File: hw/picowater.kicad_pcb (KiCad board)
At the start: 2 copper layers, 74.3 x 55.5 mm, 19 parts, among them J1 GPIO Pins, J2 Power In, J3 +5V Pins, J4 UART, J5 Power Out, J6 RTC, J7 GPIO2, U1 Pico

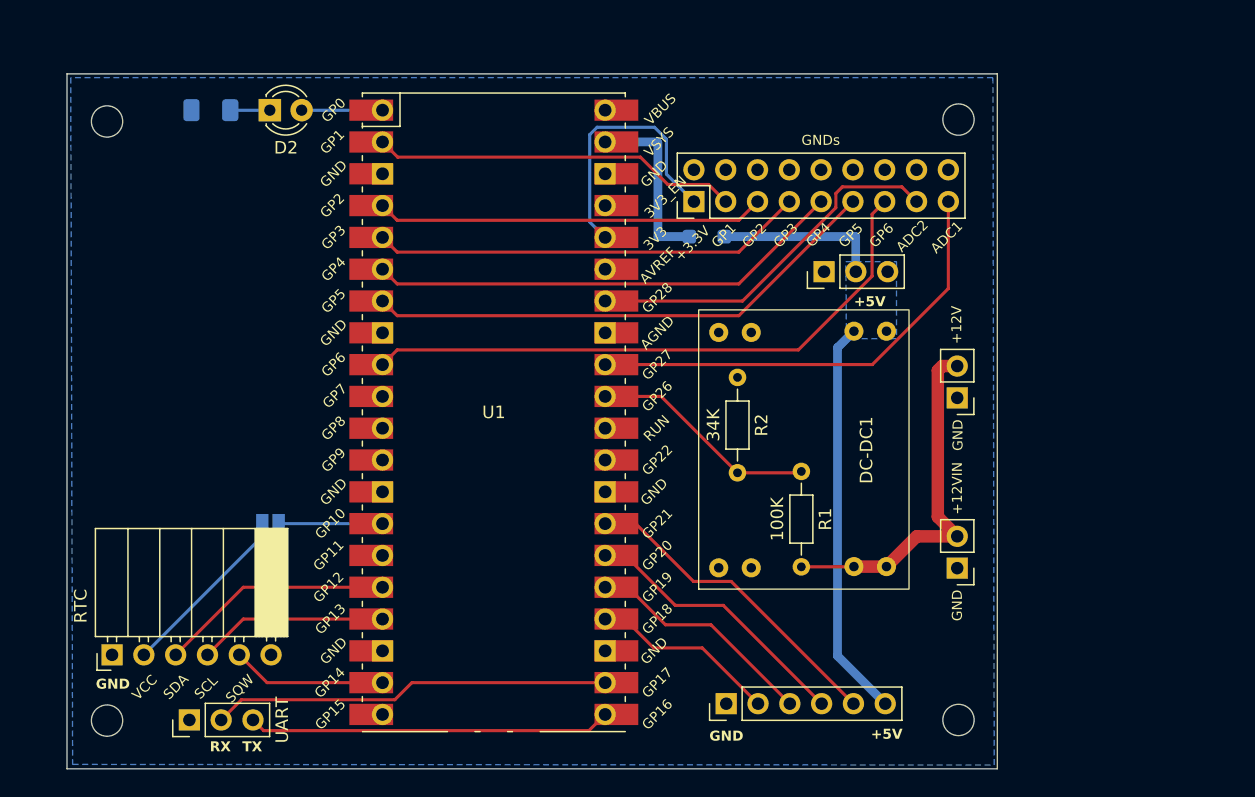
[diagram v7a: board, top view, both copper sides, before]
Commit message: [pcb] new 0.9 release with many changes
- onboard DC-DC converter
- onboard RTC
- onboard Relay circuit
- new connectors
- others
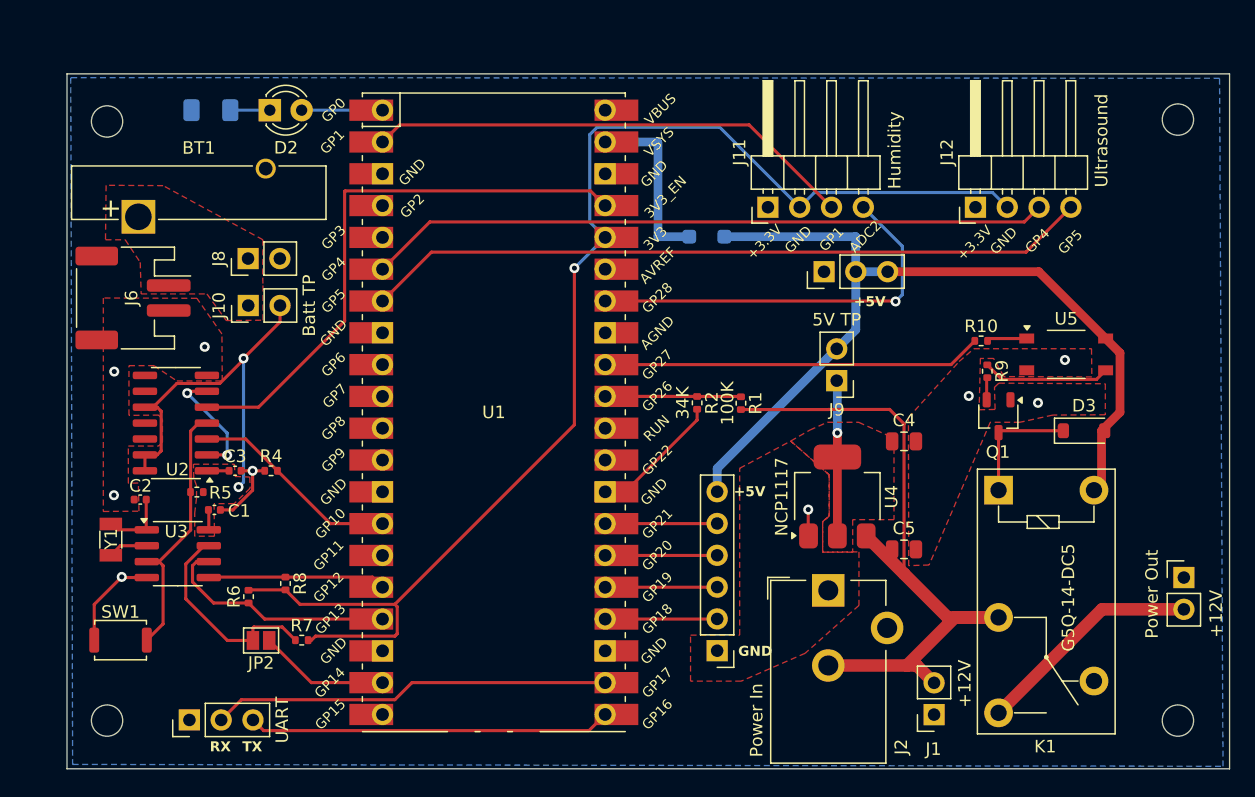
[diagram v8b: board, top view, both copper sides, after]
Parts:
- removed DC-DC1: ~, Lunasys_Library:MP1584EN DC-DC 3A Step-Down
- removed JP1: VCC solder jump, Jumper:SolderJumper-2_P1.3mm_Open_Pad1.0x1.5mm
- added BT1: Battery_Cell, Battery:Battery_Panasonic_CR2032-VS1N_Vertical_CircularHoles, F.Cu at (60.5, 79.5)
- added C1: 100nF, Capacitor_SMD:C_0402_1005Metric, F.Cu at (66.6, 102.9)
- added C2: 22pF, Capacitor_SMD:C_0402_1005Metric, F.Cu at (60.6, 102.1)
- added C3: 100nF, Capacitor_SMD:C_0402_1005Metric, F.Cu at (68.2, 99.8)
- added C4: 10u, Capacitor_SMD:C_0805_2012Metric, F.Cu at (121.7, 97.5)
- added C5: 10u, Capacitor_SMD:C_0805_2012Metric, F.Cu at (121.7, 106.1)
- added D3: 1N4007, Diode_SMD:D_SOD-123, F.Cu at (136.0, 96.6)
- added J10: Batt TP, Connector_PinHeader_2.54mm:PinHeader_1x02_P2.54mm_Vertical, F.Cu at (69.3, 86.6)
- added J11: Humidity, Connector_PinHeader_2.54mm:PinHeader_1x04_P2.54mm_Horizontal, F.Cu at (110.8, 78.8)
- added J12: Ultrasound, Connector_PinHeader_2.54mm:PinHeader_1x04_P2.54mm_Horizontal, F.Cu at (127.4, 78.8)
- added J8: Alt-Bat, Connector_PinHeader_2.54mm:PinHeader_1x02_P2.54mm_Vertical, F.Cu at (69.3, 82.8)
- added J9: 5V TP, Connector_PinHeader_2.54mm:PinHeader_1x02_P2.54mm_Vertical, F.Cu at (116.3, 92.6)
- added JP2: Jmp_CLKOUT, Jumper:SolderJumper-2_P1.3mm_Open_Pad1.0x1.5mm, F.Cu at (70.3, 113.3)
- added K1: G5Q-14-DC5, Relay_THT:Relay_SPDT_Omron-G5Q-1, F.Cu at (129.2, 101.3)
- added Q1: S8050, Package_TO_SOT_SMD:TSOT-23, F.Cu at (129.2, 95.4)
- added R10: 100, Resistor_SMD:R_0402_1005Metric, F.Cu at (127.8, 89.4)
- added R4: 100K, Resistor_SMD:R_0402_1005Metric, F.Cu at (71.1, 99.8)
- added R5: 10K, Resistor_SMD:R_0402_1005Metric, F.Cu at (65.2, 101.5)
- added R6: 10K, Resistor_SMD:R_0402_1005Metric, F.Cu at (69.3, 109.8)
- added R7: 10K, Resistor_SMD:R_0402_1005Metric, F.Cu at (73.5, 113.3)
- added R8: 10K, Resistor_SMD:R_0402_1005Metric, F.Cu at (72.2, 108.8)
- added R9: 220, Resistor_SMD:R_0402_1005Metric, F.Cu at (128.3, 91.8)
- added SW1: SW_Push_SLIM, Button_Switch_SMD:SW_Push_SPST_NO_Alps_SKRK, F.Cu at (59.1, 113.3)
- added U2: SN74HC74N, Package_SO:SOIC-14_3.9x8.7mm_P1.27mm, F.Cu at (63.5, 96.0)
- added U3: PCF8563T, Package_SO:SOIC-8_3.9x4.9mm_P1.27mm, F.Cu at (63.6, 106.4)
- added U4: NCP1117, Package_TO_SOT_SMD:SOT-223-3_TabPin2, F.Cu at (116.3, 101.8)
- added U5: TLP160G, Package_SO:MFSOP6-4_4.4x3.6mm_P1.27mm, F.Cu at (134.6, 90.5)
- added Y1: Crystal, Crystal:Crystal_SMD_3215-2Pin_3.2x1.5mm, F.Cu at (58.3, 105.3)
- J1: value GPIO Pins -> +12V; footprint Connector_PinHeader_2.54mm:PinHeader_2x09_P2.54mm_Vertical -> Connector_PinSocket_2.54mm:PinSocket_1x02_P2.54mm_Vertical
- J2: footprint Connector_PinHeader_2.54mm:PinHeader_1x02_P2.54mm_Vertical -> Connector_BarrelJack:BarrelJack_CUI_PJ-102AH_Horizontal
- J6: value RTC -> JST-PH2 Bat; footprint Connector_PinSocket_2.54mm:PinSocket_1x06_P2.54mm_Horizontal -> Connector_JST:JST_PH_S2B-PH-SM4-TB_1x02-1MP_P2.00mm_Horizontal
- R1, R2: footprint Resistor_THT:R_Axial_DIN0204_L3.6mm_D1.6mm_P7.62mm_Horizontal -> Resistor_SMD:R_0402_1005Metric
- moved J1 45.2 mm to (124.0, 119.3), turned to 180 degrees
- moved J6 30.6 mm to (60.1, 86.0)
- moved J5 23.1 mm to (144.0, 108.3), turned to 0 degrees
- moved H4 17.5 mm to (143.5, 119.8)
- moved H2 17.5 mm to (143.5, 71.8)
- moved J2 10.5 mm to (115.6, 109.3), turned to 0 degrees
- moved R1 7.28 mm to (108.6, 94.4)
- moved J7 4.29 mm to (106.7, 114.2), turned to 180 degrees
- moved R2 3.81 mm to (105.1, 94.4), turned to 90 degrees
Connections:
- J1 pad 1: +3.3V -> GND
- J1 pad 2: GND -> +12V
- J5 pad 2: +12V -> Net-(J5-Pin_2)
- J6 pad 1: GND -> Net-(BT1-+)
- J6 pad 2: Net-(J6-Pin_2) -> GND
- U1 pad 14: /VCC -> WORK_DONE
- U1 pad 16: /SDA -> SDA
- U1 pad 17: /SCL -> SCL
- U1 pad 19: /SQW -> SQW
- U1 pad 32: ADC1 -> GPIO27
- U1 pad 37: unconnected-(U1-3V3_EN-Pad37) -> 3V3_EN
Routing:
- net +3.3V: track 21.4 -> 104.1 mm, vias 0 -> 1
- net GPIO6: track 48.4 -> 0.00 mm
- net 3V3_EN: track 0.00 -> 45.5 mm
- net ADC1: track 36.9 -> 0.00 mm
- net +BATT: track 0.00 -> 36.1 mm, vias 0 -> 2
- net GPIO3: track 34.6 -> 0.00 mm
- net GPIO2: track 31.1 -> 0.00 mm
- net GPIO27: track 0.00 -> 30.3 mm
- net +12V: track 29.1 -> 56.7 mm
- net GND: track 0.00 -> 27.3 mm, vias 0 -> 9
- net +5V: track 45.5 -> 71.1 mm
- net 1~{PRE}: track 0.00 -> 21.0 mm
- net SCL: track 0.00 -> 19.1 mm
- net /SDA: track 18.8 -> 0.00 mm
- net Net-(J5-Pin_2): track 0.00 -> 18.2 mm
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- added copper zone on F.Cu, net +BATT
- added copper zone on F.Cu, net GND
- added copper zone on F.Cu, net Net-(BT1-+)
- added copper zone on F.Cu, net Net-(J9-Pin_1)
- removed copper zone on B.Cu, net +5V
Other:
- board size 74.3 x 55.5 mm -> 92.9 x 55.5 mm
- board text added: "v0.9"
- board text removed: "+12VIN"
- board text removed: "ADC1"
- board text removed: "GNDs"
- board text removed: "GP2"
- board text removed: "GP3"
- board text removed: "GP6"
- board text removed: "SCL"
- board text removed: "SDA"
- board text removed: "SQW"
- board text removed: "VCC"
- board text removed: "v0.3"
